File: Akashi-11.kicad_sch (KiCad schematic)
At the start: 2 parts, among them CN10 PPPC192LFBN-RC, CN7 PPPC192LFBN-RC

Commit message: Rough schematics drawing.
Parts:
- added C? (x4): C, symbol Device:C
- added C? (x2): C_Small, symbol Device:C_Small
- added C? (x2): C_Polarized_Small, symbol Device:C_Polarized_Small
- added D?: D_Schottky, symbol Device:D_Schottky
- added D?: D, symbol Device:D
- added J?: Conn_02x20_Odd_Even, symbol Connector_Generic:Conn_02x20_Odd_Even
- added L? (x2): LQH5BPN100M38L, IND_LQH5BPN_MUR, symbol LQH5BPN100M:LQH5BPN100M38L
- added R? (x3): R, symbol Device:R
- added U?: TPS613221ADBV, Package_TO_SOT_SMD:SOT-23-5, symbol Regulator_Switching:TPS613221ADBV
- added U?: TLV61046ADB, Package_TO_SOT_SMD:SOT-23-6, symbol Regulator_Switching:TLV61046ADB
- added U?: MAX6934AQH+D, 21-0049_Q44+1_MXM, symbol MA6934AQH:MAX6934AQH+D
- added U?: MAX4719EUB+, 21-0061L, symbol MAX4719EUB:MAX4719EUB+
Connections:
- net LOAD: now reaches CN7.1 (Pin_1)
- net LOAD: now also U?.24 (LOAD)
- net +3V3: now reaches CN7.12 (Pin_12)
- net +3V3: now also CN7.16 (Pin_16), C?.1, C?.1, U?.1 (V+), U?.10 (NO2), U?.2 (NO1), U?.4 (VOUT), U?.44 (VCC)
- net GND: now reaches CN7.19 (Pin_19)
- net GND: now also CN10.20 (Pin_20), CN10.32 (Pin_32), CN10.9 (Pin_9), CN7.20 (Pin_20), CN7.22 (Pin_22), CN7.8 (Pin_8), C?.2, C?.2, C?.2, C?.2, C?.2, C?.2, C?.2, D?.1 (K), J?.40 (Pin_40), R?.2, U?.2 (GND), U?.2 (GND), U?.22 (GND), U?.5 (NC1), U?.6 (GND), U?.7 (NC2)
- net BLANK: now reaches CN7.3 (Pin_3)
- net BLANK: now also U?.21 (BLANK)
- net SPI1_MOSI: now reaches CN10.12 (Pin_12)
- net SPI1_MOSI: now also U?.43 (DIN)
- net TIM1_CH1N: now reaches CN10.15 (Pin_15)
- net TIM1_CH1N: now also U?.4 (IN1)
- net TIM2_CH1: now reaches CN10.21 (Pin_21)
- net TIM2_CH1: now also C?.2
- net TIM1_CH1: now reaches CN10.23 (Pin_23)
- net TIM1_CH1: now also U?.8 (IN2)
- net SPI1_SCK: now reaches CN10.36 (Pin_36)
- net SPI1_SCK: now also U?.23 (CLK)
- new net: L?.1, U?.1 (SW) (x2)
- new net: R?.1, R?.2, U?.3 (FB)
- new net: C?.1, D?.1 (K), D?.2 (A)
- new net: R?.2, U?.3 (COM1)
- new net +24V: C?.1, C?.1, R?.1, U?.1 (VBB), U?.5 (VOUT)
- new net +BATT: C?.1, C?.1, J?.38 (Pin_38), L?.2, L?.2, U?.4 (EN), U?.6 (VI)
- new net -2V5: C?.1, D?.2 (A), U?.18 (VSS)
- new net D0: J?.28 (Pin_28), J?.35 (Pin_35)
- new net D1: J?.26 (Pin_26), J?.31 (Pin_31)
- new net D2: J?.24 (Pin_24), J?.27 (Pin_27)
- new net D3: J?.22 (Pin_22), J?.23 (Pin_23)
- new net D4: J?.19 (Pin_19), J?.20 (Pin_20)
- new net D5: J?.17 (Pin_17), J?.18 (Pin_18)
- new net D6: J?.13 (Pin_13), J?.16 (Pin_16)
- new net D7: J?.14 (Pin_14), J?.9 (Pin_9)
- new net D8: J?.12 (Pin_12), J?.5 (Pin_5)
- new net DP: J?.25 (Pin_25)
- new net H1: J?.1 (Pin_1), R?.1
- new net H2: J?.2 (Pin_2), U?.9 (COM2)
- new net KEY1: J?.6 (Pin_6)
- new net KEY2: J?.8 (Pin_8)
- new net KEY3: J?.10 (Pin_10)
- new net Seg_a: J?.3 (Pin_3)
- new net Seg_b: J?.33 (Pin_33)
- new net Seg_c: J?.29 (Pin_29)
- new net Seg_d: J?.21 (Pin_21)
- new net Seg_e: J?.15 (Pin_15)
- new net Seg_f: J?.11 (Pin_11)
- new net Seg_g: J?.7 (Pin_7)
- no-connect marks 0 -> 7
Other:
- note added: "PA12"
- note added: "PA7"
- note added: "PA8"
- note added: "PA9"
- note added: "PC10"
- note added: "PC12"
- note added: "PD8"
- moved on the sheet: CN10, CN7

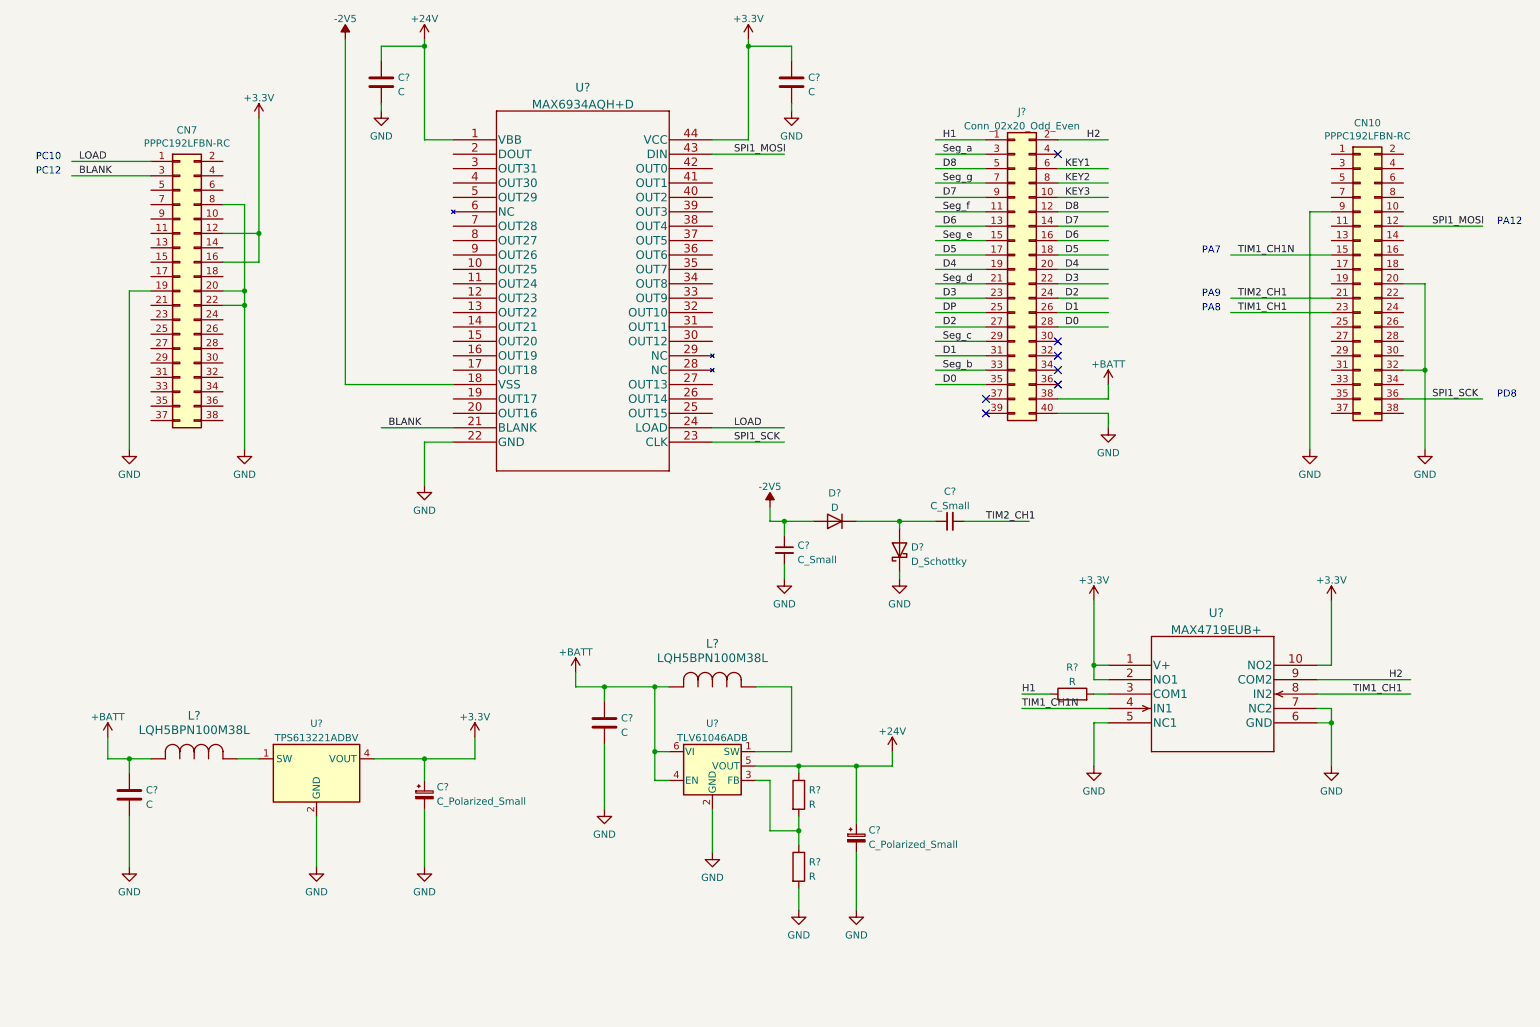
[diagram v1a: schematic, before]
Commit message: Add bypass capacitor to -2.5V of the VFD driver.
Schematics layout is refined.
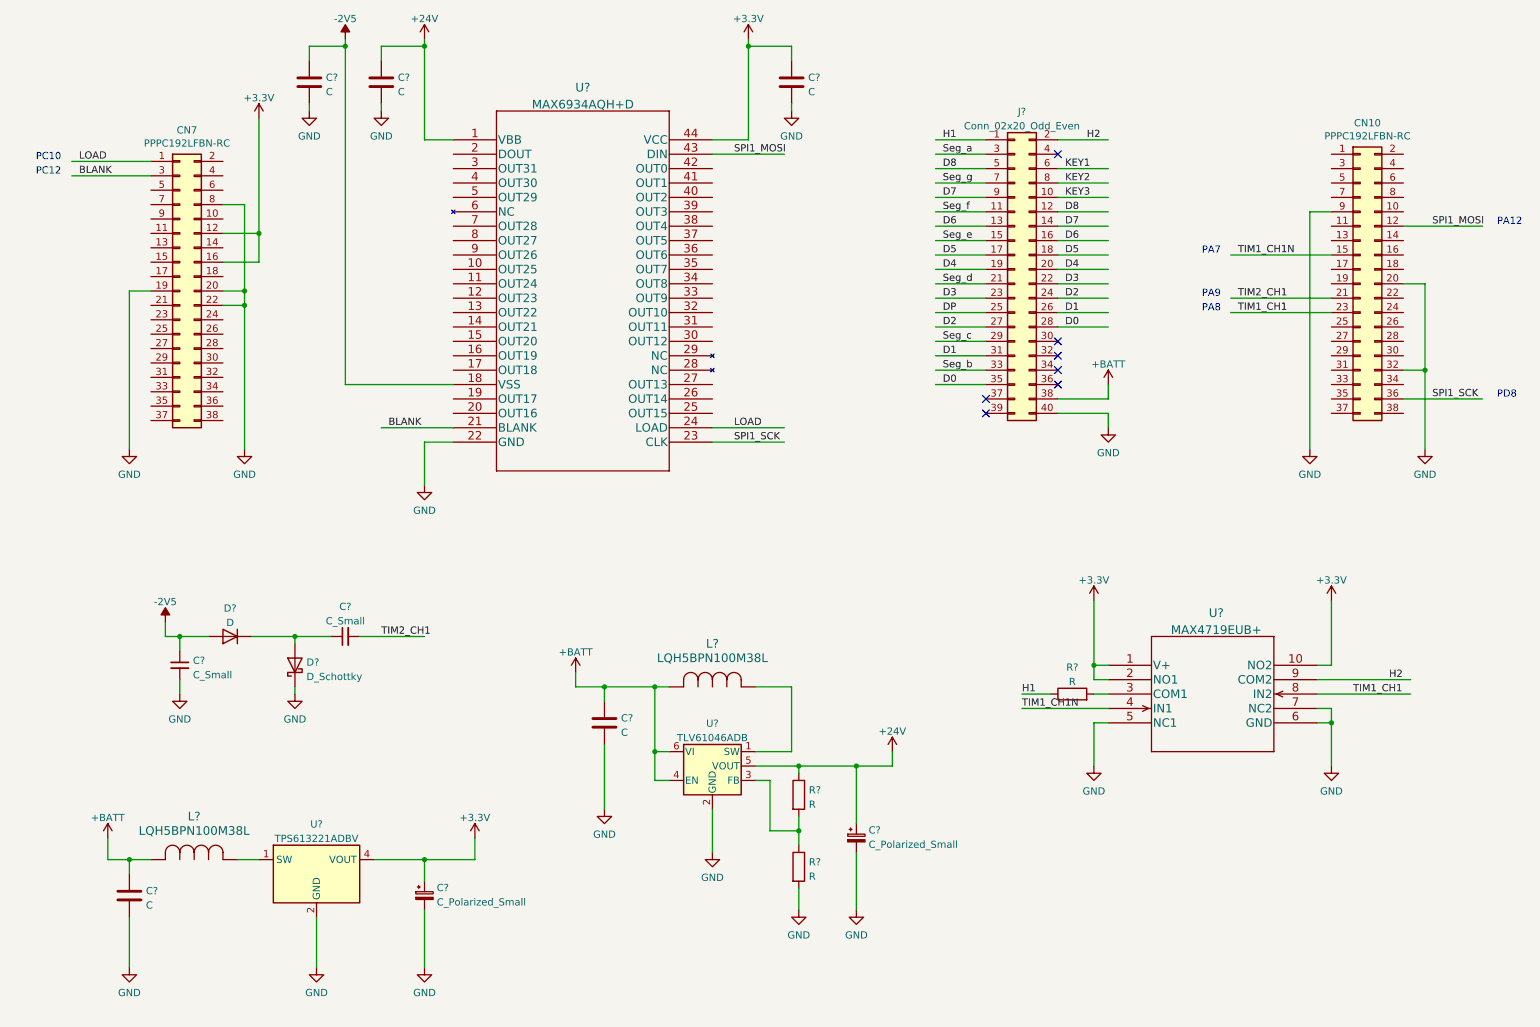
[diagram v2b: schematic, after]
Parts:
- added C?: C, symbol Device:C
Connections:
- net -2V5: now also C?.1
- net GND: now also C?.2
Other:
- moved on the sheet: C?, D?, L?, U?

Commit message: ERC finished
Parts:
- removed D?: D, symbol Device:D
- removed L? (x2): LQH5BPN100M38L, IND_LQH5BPN_MUR, symbol LQH5BPN100M:LQH5BPN100M38L
- added D1: D_Schottky, symbol Device:D_Schottky
- added D3: LED, symbol Device:LED
- added L1: LQH5BPN4R7N38L, symbol Device:L
- added L2: LQH5BPN100M38L, symbol Device:L
- added R1: 1k, symbol Device:R
- added R5: 330, symbol Device:R
- added SW1: SW, symbol Switch:SW_MEC_5G
- C1, C3, C5, C7, C8: renamed from C?; value C -> 0.1u
- C2, C4: renamed from C?; value C_Small -> 1u
- C6: renamed from C?; value C_Polarized_Small -> 22u
- C9: renamed from C?; value C_Polarized_Small -> 10u
- R2: renamed from R?; value R -> 61.9
- R3: renamed from R?; value R -> 2.15
- R4: renamed from R?; value R -> 39
- gave numbers to parts that had none: 6
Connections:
- net +BATT: now also L1.1, L2.1
- net -2V5: now also D1.2 (A)
- net D0: now also CN10.11 (Pin_11), U1.42 (OUT0)
- net D1: now also CN10.13 (Pin_13), U1.40 (OUT2)
- net D2: now also CN10.16 (Pin_16), U1.38 (OUT4)
- net D3: now also CN10.17 (Pin_17), U1.36 (OUT6)
- net D4: now also CN10.19 (Pin_19), U1.34 (OUT8)
- net D5: now also CN10.22 (Pin_22), U1.33 (OUT9)
- net D6: now also CN10.24 (Pin_24), U1.31 (OUT11)
- net D7: now also CN10.25 (Pin_25), U1.27 (OUT13)
- net D8: now also CN10.27 (Pin_27), U1.25 (OUT15)
- net DP: now also U1.37 (OUT5)
- net GND: now also R1.2, SW1.1 (A), SW1.2 (A)
- net KEY1: now also CN10.33 (Pin_33)
- net KEY2: now also CN10.31 (Pin_31)
- net KEY3: now also CN10.29 (Pin_29)
- net Seg_a: now also U1.20 (OUT16)
- net Seg_b: now also U1.41 (OUT1)
- net Seg_c: now also U1.39 (OUT3)
- net Seg_d: now also U1.35 (OUT7)
- net Seg_e: now also U1.32 (OUT10)
- net Seg_f: now also U1.30 (OUT12)
- net Seg_g: now also U1.26 (OUT14)
- net TIM2_CH1: now also R5.2; no longer C4.2
- net at CN7.14 (Pin_14): now also SW1.3 (B), SW1.4 (B)
- net at CN7.2 (Pin_2): now also D3.2 (A)
- net at U4.1 (SW): now also L2.2
- net at C4.1: now also R5.1; no longer D2.2 (A)
- net at U3.1 (SW): now also L1.2
- new net: C4.2, D1.1 (K), D2.2 (A)
- new net: D3.1 (K), R1.1
- no-connect marks 7 -> 69
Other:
- note added: "PA10"
- note added: "PA5"
- note added: "PA6"
- note added: "PB0"
- note added: "PB14"
- note added: "PB2"
- note added: "PB3"
- note added: "PB4"
- note added: "PB5"
- note added: "PB6"
- note added: "PC1"
- note added: "PC11"
- note added: "PC7"
- note added: "R2 < 80kOhm to make IR2 > 100 FB pin leakage. Vfb = 795mV R1=(Vout/Vfb-1)R2= 29.2R2. 61.9=28.8*2.15"
- note added: "RESET"
- note added: "STATUS"
- note added: "TC=0.3mSec"
- moved on the sheet: C2, C4, D2

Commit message: Initial layout of PCB.
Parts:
- C1, C2, C3, C4, C5, C7, C8, D1, D2, R1, R2, R3, R4, R5: footprint (none) -> Capacitor_SMD:C_0603_1608Metric_Pad1.08x0.95mm_HandSolder
- C6, C9: footprint (none) -> Capacitor_THT:CP_Radial_D5.0mm_P2.50mm
- D3: footprint (none) -> LED_THT:LED_D4.0mm
- J1: footprint (none) -> Connector_PinHeader_2.54mm:PinHeader_2x20_P2.54mm_Vertical
- L1, L2: footprint (none) -> LOCAL_LIB:LQH5BPN100M38L
- SW1: footprint (none) -> Button_Switch_THT:SW_TH_Tactile_Omron_B3F-10xx
- U1: footprint 21-0049_Q44+1_MXM -> Package_LCC:PLCC-44_THT-Socket
- U2: footprint 21-0061L -> LOCAL_LIB:MAX4719EUB

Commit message: Routing finished
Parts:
- added JP1, JP2: Jumper_2_Bridged, Jumper:SolderJumper-2_P1.3mm_Bridged_RoundedPad1.0x1.5mm, symbol Jumper:Jumper_2_Bridged
- added TP1, TP10, TP11, TP12, TP13, TP2, TP3, TP4, TP5, TP6, TP7, TP8, TP9: TestPoint, TestPoint:TestPoint_Loop_D1.80mm_Drill1.0mm_Beaded, symbol Connector:TestPoint
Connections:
- net +24V: now also JP2.2 (B); no longer C9.1, R2.1, U4.5 (VOUT)
- net +3V3: now also JP1.2 (B); no longer C6.1, U3.4 (VOUT)
- net -2V5: now also TP2.1
- net BLANK: now also TP9.1
- net D0: no longer CN10.11 (Pin_11), J1.28 (Pin_28)
- net D1: no longer CN10.13 (Pin_13), J1.26 (Pin_26)
- net D2: no longer CN10.16 (Pin_16), J1.24 (Pin_24)
- net D3: no longer CN10.17 (Pin_17), J1.22 (Pin_22)
- net D4: no longer CN10.19 (Pin_19), J1.20 (Pin_20)
- net D5: no longer CN10.22 (Pin_22), J1.18 (Pin_18)
- net D6: no longer CN10.24 (Pin_24), J1.16 (Pin_16)
- net D7: no longer CN10.25 (Pin_25), J1.14 (Pin_14)
- net D8: no longer CN10.27 (Pin_27), J1.12 (Pin_12)
- net GND: now also TP4.1
- net H1: now also TP11.1
- net H2: now also TP12.1
- net LOAD: now also TP8.1
- net SPI1_MOSI: now also TP6.1
- net SPI1_SCK: now also TP5.1
- net TIM1_CH1: now also TP13.1
- net TIM1_CH1N: now also TP10.1
- net TIM2_CH1: now also TP1.1
- new net: C6.1, JP1.1 (A), TP3.1, U3.4 (VOUT)
- new net: C9.1, JP2.1 (A), R2.1, TP7.1, U4.5 (VOUT)
- new net KD0: CN10.11 (Pin_11), J1.28 (Pin_28)
- new net KD1: CN10.13 (Pin_13), J1.26 (Pin_26)
- new net KD2: CN10.16 (Pin_16), J1.24 (Pin_24)
- new net KD3: CN10.17 (Pin_17), J1.22 (Pin_22)
- new net KD4: CN10.19 (Pin_19), J1.20 (Pin_20)
- new net KD5: CN10.22 (Pin_22), J1.18 (Pin_18)
- new net KD6: CN10.24 (Pin_24), J1.16 (Pin_16)
- new net KD7: CN10.25 (Pin_25), J1.14 (Pin_14)
- new net KD8: CN10.27 (Pin_27), J1.12 (Pin_12)

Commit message: Add EN24 signal and description of README
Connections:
- net +BATT: no longer U4.4 (EN)
- net EN24: now reaches CN7.2 (Pin_2)
- net EN24: now also U4.4 (EN); no longer D3.2 (A)
- net STATUS: now reaches CN7.4 (Pin_4)
- net STATUS: now also D3.2 (A)
- no-connect marks 69 -> 68
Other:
- note added: "PD2"
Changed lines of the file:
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@@
   (junction (at 144.78 20.32) (diameter 0) (color 0 0 0 0)
-  )
-  (junction (at 128.27 144.78) (diameter 0) (color 0 0 0 0)
   )
   (junction (at 128.27 133.35) (diameter 0) (color 0 0 0 0)
@@
   (no_connect (at 52.07 78.74))
   (no_connect (at 52.07 81.28))
-  (no_connect (at 52.07 43.18))
   (no_connect (at 52.07 45.72))
   (no_connect (at 52.07 50.8))
@@
     (stroke (width 0) (type default) (color 0 0 0 0))
   )
+  (wire (pts (xy 52.07 43.18) (xy 67.31 43.18))
+    (stroke (width 0) (type default) (color 0 0 0 0))
+  )
   (wire (pts (xy 245.11 129.54) (xy 247.65 129.54))
     (stroke (width 0) (type default) (color 0 0 0 0))
@@
     (stroke (width 0) (type default) (color 0 0 0 0))
   )
+  (wire (pts (xy 67.31 43.18) (xy 67.31 49.53))
+    (stroke (width 0) (type default) (color 0 0 0 0))
+  )
   (wire (pts (xy 245.11 134.62) (xy 265.43 134.62))
     (stroke (width 0) (type default) (color 0 0 0 0))
@@
     (stroke (width 0) (type default) (color 0 0 0 0))
   )
-  (wire (pts (xy 130.81 149.86) (xy 128.27 149.86))
-    (stroke (width 0) (type default) (color 0 0 0 0))
-  )
   (wire (pts (xy 177.8 44.45) (xy 186.69 44.45))
     (stroke (width 0) (type default) (color 0 0 0 0))
@@
     (stroke (width 0) (type default) (color 0 0 0 0))
   )
+  (wire (pts (xy 124.46 149.86) (xy 130.81 149.86))
+    (stroke (width 0) (type default) (color 0 0 0 0))
+  )
   (wire (pts (xy 87.63 163.83) (xy 90.17 163.83))
     (stroke (width 0) (type default) (color 0 0 0 0))
@@
     (stroke (width 0) (type default) (color 0 0 0 0))
   )
-  (wire (pts (xy 67.31 40.64) (xy 67.31 49.53))
-    (stroke (width 0) (type default) (color 0 0 0 0))
-  )
   (wire (pts (xy 199.39 57.15) (xy 208.28 57.15))
     (stroke (width 0) (type default) (color 0 0 0 0))
@@
   )
   (wire (pts (xy 254 140.97) (xy 254 143.51))
-    (stroke (width 0) (type default) (color 0 0 0 0))
-  )
-  (wire (pts (xy 128.27 149.86) (xy 128.27 144.78))
     (stroke (width 0) (type default) (color 0 0 0 0))
   )
@@
     (effects (font (size 1.27 1.27)) (justify left bottom))
   )
-  (text "PC11" (at 62.23 43.18 0)
+  (text "PC11" (at 68.58 40.64 0)
     (effects (font (size 1.27 1.27)) (justify left bottom))
   )
@@
     (effects (font (size 1.27 1.27)) (justify left bottom))
   )
+  (text "PD2" (at 68.58 43.18 0)
+    (effects (font (size 1.27 1.27)) (justify left bottom))
+  )
   (text "PA10" (at 224.79 80.01 0)
     (effects (font (size 1.27 1.27)) (justify left bottom))
@@
     (effects (font (size 1.27 1.27)) (justify left bottom))
   )
+  (label "STATUS" (at 59.69 43.18 0)
+    (effects (font (size 1.27 1.27)) (justify left bottom))
+  )
   (label "KEY2" (at 231.14 77.47 0)
     (effects (font (size 1.27 1.27)) (justify left bottom))
@@
     (effects (font (size 1.27 1.27)) (justify left bottom))
   )
+  (label "EN24" (at 125.73 149.86 0)
+    (effects (font (size 1.27 1.27)) (justify left bottom))
+  )
   (label "KD4" (at 200.66 59.69 0)
     (effects (font (size 1.27 1.27)) (justify left bottom))
@@
   )
   (label "TIM1_CH1N" (at 193.04 137.16 0)
+    (effects (font (size 1.27 1.27)) (justify left bottom))
+  )
+  (label "EN24" (at 59.69 40.64 0)
     (effects (font (size 1.27 1.27)) (justify left bottom))
   )
@@
   )
   (symbol (lib_id "Connector:TestPoint") (at 114.3 149.86 0) (unit 1)
-    (in_bom yes) (on_board yes) (fields_autoplaced)
+    (in_bom yes) (on_board yes)
     (property "Reference" "TP4" (id 0) (at 115.697 145.7233 0)
       (effects (font (size 1.27 1.27)) (justify left))
     )
-    (property "Value" "TestPoint" (id 1) (at 115.697 148.2602 0)
+    (property "Value" "TestPoint" (id 1) (at 105.41 144.78 0)
       (effects (font (size 1.27 1.27)) (justify left))
     )
@@
   )
   (symbol (lib_id "Connector:TestPoint") (at 34.29 124.46 0) (unit 1)
-    (in_bom yes) (on_board yes) (fields_autoplaced)
-    (property "Reference" "TP1" (id 0) (at 35.687 120.3233 0)
+    (in_bom yes) (on_board yes)
+    (property "Reference" "TP1" (id 0) (at 30.48 120.65 0)
       (effects (font (size 1.27 1.27)) (justify left))
     )
-    (property "Value" "TestPoint" (id 1) (at 35.687 122.8602 0)
+    (property "Value" "TestPoint" (id 1) (at 29.21 118.11 0)
       (effects (font (size 1.27 1.27)) (justify left))
     )
